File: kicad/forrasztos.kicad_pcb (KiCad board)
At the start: 2 copper layers, 90 parts, among them J1 24V+-, J2 Conn_01x04_Pin, J3 Conn_01x20_Pin, J4 Conn_01x06_Pin, J5 Conn_01x04_Pin, Q1 AOD409, Q2 MMST2222A, Q3 AOD409, Q4 MMST2222A, SW1 RotaryEncoder_Switch, SW2 SW_Push, SW3 SW_Push, U1 AP63205WU, U2 MCP6004, U3 AP63203WU, U4 24LC00, U5 STM32F103C8Tx, Y1 ATS080B

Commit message: redone pcb
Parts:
- removed the C13 at (153.3, 94.8)
- removed the C14 at (153.3, 90.2)
- removed the C15 at (145.3, 83.0)
- removed the C16 at (143.3, 87.0)
- removed the R6 at (162.6, 86.7)
- removed the R7 at (159.8, 86.8)
- added C13: 100n, Capacitor_SMD:C_0805_2012Metric_Pad1.18x1.45mm_HandSolder, F.Cu at (97.8, 86.4)
- added C13: 100n, Capacitor_SMD:C_0805_2012Metric_Pad1.18x1.45mm_HandSolder, F.Cu at (145.9, 90.6)
- added C14: 100n, Capacitor_SMD:C_0805_2012Metric_Pad1.18x1.45mm_HandSolder, F.Cu at (97.8, 89.4)
- added C14: 100n, Capacitor_SMD:C_0805_2012Metric_Pad1.18x1.45mm_HandSolder, F.Cu at (147.9, 80.4)
- added C15: 100n, Capacitor_SMD:C_0805_2012Metric_Pad1.18x1.45mm_HandSolder, F.Cu at (97.8, 92.4)
- added C15: 100n, Capacitor_SMD:C_0805_2012Metric_Pad1.18x1.45mm_HandSolder, F.Cu at (137.5, 77.1)
- added C16: 100n, Capacitor_SMD:C_0805_2012Metric_Pad1.18x1.45mm_HandSolder, F.Cu at (97.8, 95.4)
- added C16: 100n, Capacitor_SMD:C_0805_2012Metric_Pad1.18x1.45mm_HandSolder, F.Cu at (134.4, 79.4)
- added R42: 82k, Resistor_SMD:R_0805_2012Metric_Pad1.20x1.40mm_HandSolder, F.Cu at (156.3, 101.5)
- added R43: 33K, Resistor_SMD:R_0805_2012Metric_Pad1.20x1.40mm_HandSolder, F.Cu at (156.3, 104.5)
- added R44: 1.5K, Resistor_SMD:R_0805_2012Metric_Pad1.20x1.40mm_HandSolder, F.Cu at (147.9, 98.8)
- added R6: 4k7, Resistor_SMD:R_0805_2012Metric_Pad1.20x1.40mm_HandSolder, F.Cu at (155.3, 90.6)
- added R6: 4k7, Resistor_SMD:R_0805_2012Metric_Pad1.20x1.40mm_HandSolder, F.Cu at (102.6, 86.3)
- added R7: 4k7, Resistor_SMD:R_0805_2012Metric_Pad1.20x1.40mm_HandSolder, F.Cu at (102.6, 89.3)
- added R7: 4k7, Resistor_SMD:R_0805_2012Metric_Pad1.20x1.40mm_HandSolder, F.Cu at (153.2, 90.6)
- C11, C12, FB2, J1, R12, R17, R38, R41: moved to F.Cu
- J2, J5: footprint Connector_PinHeader_2.54mm:PinHeader_1x04_P2.54mm_Vertical -> Connector_PinHeader_2.54mm:PinHeader_2x04_P2.54mm_Vertical
- moved R2 169.4 mm to (176.3, 95.6), turned to 90 degrees
- moved J1 168.3 mm to (202.6, 81.5)
- moved R1 166.8 mm to (171.9, 95.6), turned to 90 degrees
- moved R3 166.2 mm to (174.2, 95.6), turned to 90 degrees
- moved C7 145.8 mm to (187.4, 70.1), turned to 90 degrees
- moved RV1 145.5 mm to (194.3, 72.4)
- moved C8 144.9 mm to (186.1, 74.0), turned to 90 degrees
- moved J5 143.9 mm to (173.5, 118.6), turned to -90 degrees
- moved C2 143.0 mm to (176.8, 74.0)
- moved C3 137.4 mm to (172.2, 73.8), turned to 90 degrees
- moved C4 133.9 mm to (169.6, 73.8), turned to 90 degrees
- moved C18 132.4 mm to (172.3, 86.6), turned to 180 degrees
- moved C1 129.5 mm to (160.5, 74.4), turned to 180 degrees
- moved C17 128.9 mm to (172.3, 84.3), turned to 180 degrees
- moved Q3 124.7 mm to (241.7, 71.7)
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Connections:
- REF** pad 1: (no net) -> Earth_Protective
- U5 pad 18: unconnected-(U5-PB0-Pad18) -> /LCD_CS1
- U5 pad 19: unconnected-(U5-PB1-Pad19) -> /LCD_CS2
- U5 pad 29: /LCD_CS1 -> /LCD_E
- U5 pad 30: /LCD_CS2 -> /LCD_RW
- U5 pad 31: /LCD_E -> /LCD_DI
- U5 pad 32: /LCD_RW -> /USB_DM
- U5 pad 33: /LCD_DI -> /USB_DP
- U5 pad 38: unconnected-(U5-PA15-Pad38) -> /USB_SNS
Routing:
- net GND: track 203.4 -> 388.4 mm, vias 9 -> 10
- net +5V: track 7.14 -> 117.2 mm, vias 0 -> 1
- net /ENC_B: track 0.00 -> 81.9 mm, vias 0 -> 2
- net /ENC_A: track 0.00 -> 81.2 mm, vias 0 -> 2
- net /ENC_SW: track 9.98 -> 87.7 mm, vias 0 -> 2
- net /LCD_VOUT: track 0.00 -> 69.8 mm, vias 0 -> 1
- net /CH2_AMP_N: track 59.6 -> 0.00 mm, vias 3 -> 0
- net /LCD_D2: track 5.43 -> 56.5 mm, vias 0 -> 1
- net /LCD_DI: track 0.00 -> 50.1 mm, vias 0 -> 1
- net /LCD_RST: track 6.50 -> 56.6 mm, vias 0 -> 1
- net /LCD_RW: track 0.00 -> 47.6 mm, vias 0 -> 1
- net /LCD_D3: track 4.60 -> 52.1 mm, vias 0 -> 1
- net /LCD_E: track 0.00 -> 46.7 mm, vias 0 -> 1
- net /LCD_V0: track 0.00 -> 45.7 mm, vias 0 -> 1
- net /LCD_D7: track 0.00 -> 42.0 mm, vias 0 -> 1
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
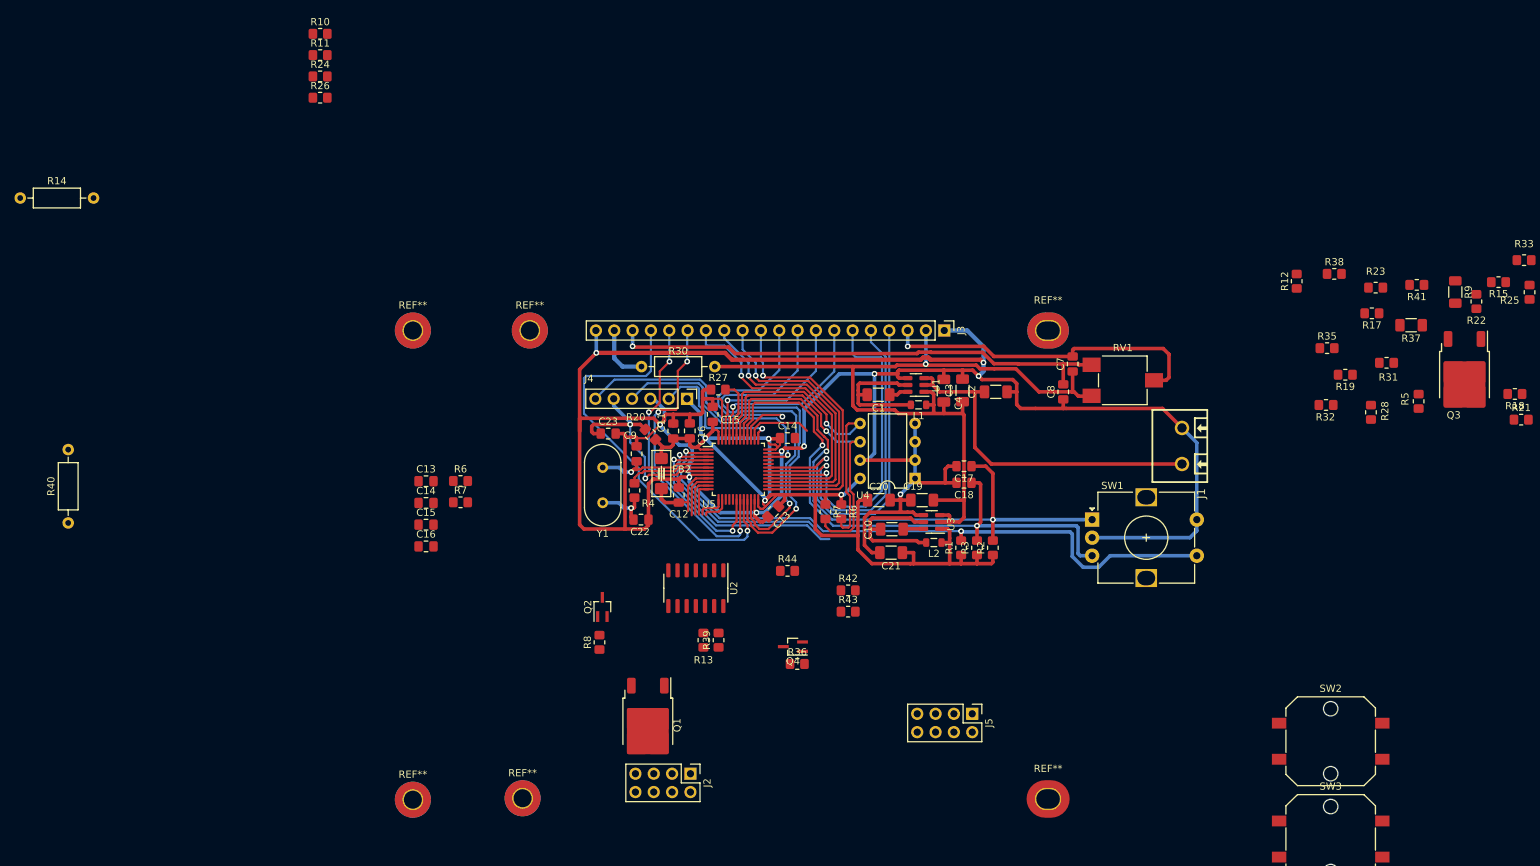
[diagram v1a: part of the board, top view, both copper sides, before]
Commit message: fixed footprints, power part done
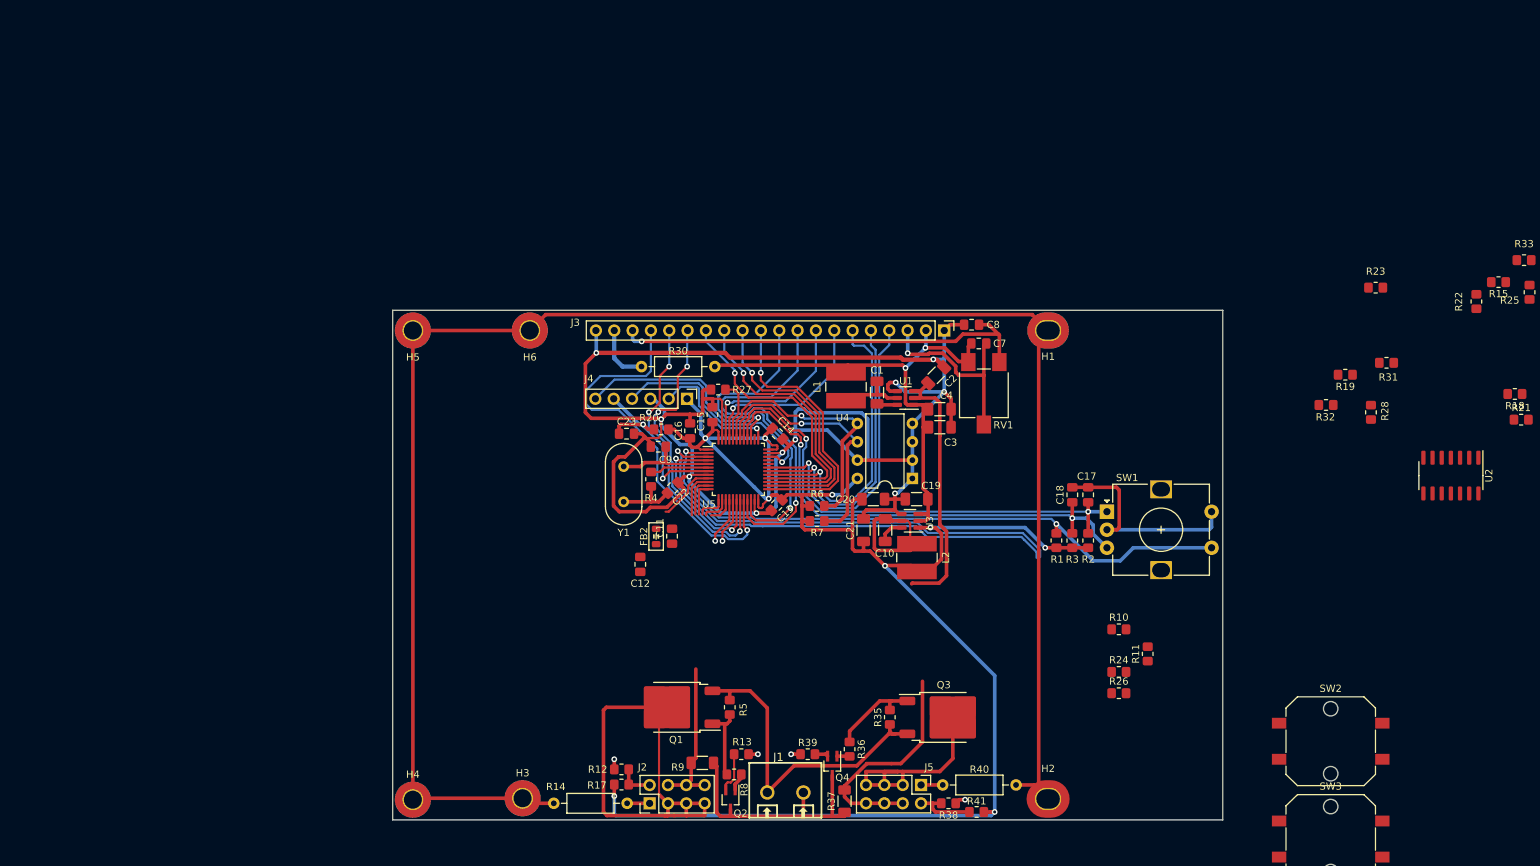
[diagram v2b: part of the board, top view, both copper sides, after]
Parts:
- removed the C13 at (145.9, 90.6)
- removed the C14 at (147.9, 80.4)
- removed the C15 at (137.5, 77.1)
- removed the C16 at (134.4, 79.4)
- removed R42: 82k, Resistor_SMD:R_0805_2012Metric_Pad1.20x1.40mm_HandSolder
- removed R43: 33K, Resistor_SMD:R_0805_2012Metric_Pad1.20x1.40mm_HandSolder
- removed R44: 1.5K, Resistor_SMD:R_0805_2012Metric_Pad1.20x1.40mm_HandSolder
- removed the R6 at (155.3, 90.6)
- removed the R7 at (153.2, 90.6)
- removed REF** (x4): MountingHole_2.5mm_Pad_TopBottom, MountingHole:MountingHole_2.5mm_Pad_TopBottom
- removed REF**: MountingHoleOval_3.27x2.7mm, forrasztos_library:MountingHoleOval_3.27x2.7mm
- removed REF**: MountingHoleOval_3.27x2.5mm, forrasztos_library:MountingHoleOval_3.27x2.5mm
- added H1: MountingHole_Pad, forrasztos_library:MountingHoleOval_3.27x2.5mm, F.Cu at (184.0, 65.5)
- added H2: MountingHole_Pad, forrasztos_library:MountingHoleOval_3.27x2.7mm, F.Cu at (184.0, 130.4)
- added H3: MountingHole_Pad, MountingHole:MountingHole_2.5mm_Pad_TopBottom, F.Cu at (111.2, 130.3)
- added H4: MountingHole_Pad, MountingHole:MountingHole_2.5mm_Pad_TopBottom, F.Cu at (96.0, 130.5)
- added H5: MountingHole_Pad, MountingHole:MountingHole_2.5mm_Pad_TopBottom, F.Cu at (96.0, 65.5)
- added H6: MountingHole_Pad, MountingHole:MountingHole_2.5mm_Pad_TopBottom, F.Cu at (112.2, 65.5)
- FB2: footprint PCM_Ferrite_SMD_Handsoldering_AKL:Ferrite_1806_4516Metric_Pad1.57x1.80mm_BigPads -> PCM_Ferrite_SMD_Handsoldering_AKL:Ferrite_0805_2012Metric
- J2, J5: value Conn_01x04_Pin -> Conn_02x04_Pin
- L1, L2: footprint Inductor_SMD:L_0805_2012Metric -> Inductor_SMD:L_TracoPower_TCK-047_5.2x5.8mm
- Q1, Q3: footprint Library:TO-252-2-custom -> forrasztos_library:TO-252-2-custom
- moved R11 141.5 mm to (197.8, 110.3), turned to 90 degrees
- moved R10 138.0 mm to (193.8, 106.9)
- moved R24 138.0 mm to (193.8, 112.8)
- moved R26 138.0 mm to (193.8, 115.8)
- moved R40 136.2 mm to (179.6, 128.5), turned to 180 degrees
- moved R9 123.0 mm to (136.1, 125.4), turned to 180 degrees
- moved R17 122.8 mm to (124.9, 128.4)
- moved R12 115.4 mm to (124.9, 126.3), turned to 0 degrees
- moved R14 111.8 mm to (115.5, 131.0)
- moved U2 105.8 mm to (239.8, 85.6)
- moved R5 104.4 mm to (139.9, 117.7), turned to -90 degrees
- moved R37 102.5 mm to (155.8, 130.7), turned to 90 degrees
- moved R41 95.1 mm to (174.1, 132.2), turned to 0 degrees
- moved R38 90.8 mm to (170.2, 131.0), turned to 180 degrees
- moved Q3 86.3 mm to (169.5, 119.1), turned to 0 degrees
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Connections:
- J2 pad 1: /CH1_AMP_P -> Net-(J2-Pin_3)
- J2 pad 3: Net-(J2-Pin_3) -> /CH1_AMP_P
- J2 pad 4: Net-(J2-Pin_4) -> /CH1_AMP_N
- J2 pad 5: (no net) -> /CH1_AMP_P
- J2 pad 6: (no net) -> /CH1_AMP_N
- J2 pad 7: (no net) -> /CH1_AMP_P
- J2 pad 8: (no net) -> /CH1_AMP_N
- J5 pad 1: /CH2_AMP_P -> Net-(J5-Pin_3)
- J5 pad 2: /CH2_AMP_N -> Net-(J5-Pin_4)
- J5 pad 3: Net-(J5-Pin_3) -> /CH2_AMP_P
- J5 pad 4: Net-(J5-Pin_4) -> /CH2_AMP_N
- J5 pad 5: (no net) -> /CH2_AMP_P
- J5 pad 6: (no net) -> /CH2_AMP_N
- J5 pad 7: (no net) -> /CH2_AMP_P
- J5 pad 8: (no net) -> /CH2_AMP_N
- U5 pad 32: /USB_DM -> unconnected-(U5-PA11-Pad32)
- U5 pad 33: /USB_DP -> unconnected-(U5-PA12-Pad33)
- U5 pad 38: /USB_SNS -> unconnected-(U5-PA15-Pad38)
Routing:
- net Earth_Protective: track 0.00 -> 245.9 mm
- net +3.3V: track 137.7 -> 239.4 mm, vias 4 -> 9
- net /CH1_AMP_P: track 0.00 -> 62.1 mm
- net GND: track 388.4 -> 341.7 mm
- net +5V: track 117.2 -> 72.1 mm, vias 1 -> 2
- net +24V: track 48.2 -> 83.2 mm
- net /BTN_1: track 31.8 -> 64.0 mm
- net /CH2_AMP_N: track 0.00 -> 31.7 mm
- net /CH2_AMP_P: track 0.00 -> 31.0 mm
- net /BTN_2: track 32.8 -> 63.0 mm
- net /CH1_AMP_N: track 0.00 -> 21.7 mm
- net /LCD_V0: track 45.7 -> 26.9 mm
- net /ENC_B: track 81.9 -> 69.0 mm
- net Net-(Q3-G): track 0.00 -> 12.5 mm
- net Net-(Q1-G): track 0.00 -> 10.6 mm
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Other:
- board outline added: 115 x 70.6 mm

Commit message: finished work on pcb
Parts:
- SW2, SW3: footprint Button_Switch_SMD:SW_Push_1P1T_NO_CK_PTS125Sx43PSMTR -> Button_Switch_THT:SW_PUSH-12mm
- moved R16 157.3 mm to (104.3, 103.3), turned to 90 degrees
- moved R25 155.7 mm to (100.8, 102.1), turned to 180 degrees
- moved R34 153.9 mm to (105.7, 106.2), turned to 180 degrees
- moved R15 149.7 mm to (99.7, 88.5)
- moved R29 149.4 mm to (107.6, 104.2)
- moved R33 148.8 mm to (108.5, 102.1)
- moved R22 148.8 mm to (100.8, 104.1), turned to 0 degrees
- moved R21 140.6 mm to (110.3, 97.8), turned to 90 degrees
- moved R18 140.1 mm to (109.5, 90.6), turned to 0 degrees
- moved U2 135.7 mm to (104.6, 97.3)
- moved R31 132.1 mm to (100.7, 92.5), turned to 180 degrees
- moved R28 129.7 mm to (99.7, 90.5), turned to 180 degrees
- moved R19 128.9 mm to (101.0, 106.1)
- moved R23 125.3 mm to (108.5, 92.6), turned to 0 degrees
- moved R32 125.3 mm to (99.0, 97.0), turned to -90 degrees
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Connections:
- J2 pad 1: Net-(J2-Pin_3) -> /CH1_AMP_P
- J2 pad 2: Net-(J2-Pin_4) -> /CH1_AMP_N
- J2 pad 3: /CH1_AMP_P -> Net-(J2-Pin_3)
- J2 pad 4: /CH1_AMP_N -> Net-(J2-Pin_4)
- J5 pad 1: Net-(J5-Pin_3) -> /CH2_AMP_P
- J5 pad 2: Net-(J5-Pin_4) -> /CH2_AMP_N
- J5 pad 3: /CH2_AMP_P -> Net-(J5-Pin_3)
- J5 pad 4: /CH2_AMP_N -> Net-(J5-Pin_4)
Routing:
- net GND: track 341.7 -> 754.3 mm, vias 10 -> 14
- net Earth_Protective: track 245.9 -> 613.2 mm
- net +3.3V: track 239.4 -> 428.1 mm, vias 9 -> 11
- net /CH2_AMP_P: track 31.0 -> 103.2 mm, vias 0 -> 53
- net /CH2_AMP_N: track 31.7 -> 98.4 mm, vias 0 -> 2
- net /CH2_TILT: track 7.98 -> 73.1 mm
- net /CH1_AMP_N: track 21.7 -> 82.7 mm, vias 0 -> 2
- net /CH1_TILT: track 8.27 -> 68.7 mm
- net /CH1_CURRENT: track 4.06 -> 60.8 mm, vias 0 -> 2
- net +5V: track 72.1 -> 117.9 mm, vias 2 -> 1
- net /CH2_THERMO: track 4.03 -> 49.5 mm, vias 0 -> 2
- net /CH1_THERMO: track 5.20 -> 48.9 mm
- net /CH2_HEATER: track 7.24 -> 48.9 mm, vias 1 -> 2
- net +3.3VA: track 8.47 -> 46.1 mm, vias 0 -> 2
- net /CH2_CURRENT: track 3.79 -> 40.0 mm, vias 0 -> 2
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- added copper zone on F.Cu, net +24V
- added copper zone on B.Cu, net +3.3V
- added copper zone on F.Cu, net +3.3V
- added copper zone on F.Cu, net +5V
- added copper zone on B.Cu, net /CH1_AMP_P
- added copper zone on F.Cu, net /CH1_AMP_P
- added copper zone on B.Cu, net /CH2_AMP_P
- added copper zone on F.Cu, net /CH2_AMP_P
- added copper zone on B.Cu, net Earth_Protective
- added copper zone on B.Cu, net GND
- added copper zone on F.Cu, net GND

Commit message: revA prototype
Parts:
- added NT1: NetTie_2, NetTie:NetTie-2_SMD_Pad0.5mm, B.Cu at (147.8, 128.9)
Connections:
- H1 pad 1: Earth_Protective -> GND
- H2 pad 1: Earth_Protective -> GND
- H3 pad 1: Earth_Protective -> GND
- H4 pad 1: Earth_Protective -> GND
- H5 pad 1: Earth_Protective -> GND
- H6 pad 1: Earth_Protective -> GND
- Q2 pad 3: GND -> GNDPWR
- Q4 pad 3: GND -> GNDPWR
- R14 pad 1: Earth_Protective -> GND
- R37 pad 1: GND -> GNDPWR
- R40 pad 1: Earth_Protective -> GND
- R9 pad 1: GND -> GNDPWR
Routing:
- net Earth_Protective: track 613.2 -> 0.00 mm
- net GND: track 754.3 -> 1286.5 mm, vias 14 -> 79
- net GNDPWR: track 0.00 -> 40.6 mm, vias 0 -> 1
- net /BTN_2: track 95.9 -> 88.9 mm
- net /BTN_1: track 75.4 -> 69.5 mm
- net Net-(Q4-C): track 3.16 -> 1.76 mm
- net Net-(Q4-B): track 3.26 -> 1.86 mm
- removed copper zone on B.Cu, net Earth_Protective
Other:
- board text added: "Elkövető: Jakab Ádám"
- board text added: "SEM forrasztoállomás Rev.A"

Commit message: start port of PTDreamer repo
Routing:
- added copper zone on F.Cu, net GNDPWR
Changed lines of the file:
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@@
   (segment (start 140.5 121.7) (end 141.5 120.7) (width 0.5) (layer "B.Cu") (net 54))
   (segment (start 138.2 130.3) (end 139.7 131.8) (width 1) (layer "F.Cu") (net 55))
-  (segment (start 155.35 131.8) (end 155.8 132.25) (width 1) (layer "F.Cu") (net 55))
   (segment (start 139.7 131.8) (end 140 131.8) (width 1) (layer "F.Cu") (net 55))
   (segment (start 138.2 127.45) (end 138.2 130.3) (width 1) (layer "F.Cu") (net 55))
   (segment (start 154.1 128.481496) (end 154.1 127.13) (width 1) (layer "F.Cu") (net 55))
+  (segment (start 153.65 131.8) (end 154.1 132.25) (width 1) (layer "F.Cu") (net 55))
   (segment (start 137.7 126.95) (end 138.2 127.45) (width 1) (layer "F.Cu") (net 55))
   (segment (start 137.7 126.95) (end 137.7 125.45) (width 1) (layer "F.Cu") (net 55))
+  (segment (start 154.1 132.25) (end 155.8 132.25) (width 1) (layer "F.Cu") (net 55))
   (segment (start 137.7 125.45) (end 137.65 125.4) (width 1) (layer "F.Cu") (net 55))
   (segment (start 139.7 131.8) (end 150.781496 131.8) (width 1) (layer "F.Cu") (net 55))
-  (segment (start 150.781496 131.8) (end 155.35 131.8) (width 1) (layer "F.Cu") (net 55))
+  (segment (start 150.781496 131.8) (end 153.65 131.8) (width 1) (layer "F.Cu") (net 55))
   (segment (start 150.781496 131.8) (end 154.1 128.481496) (width 1) (layer "F.Cu") (net 55))
   (via (at 137.7 126.95) (size 0.8) (drill 0.4) (layers "F.Cu" "B.Cu") (net 55))
@@
     )
   )
-  (zone (net 11) (net_name "+3.3V") (layer "F.Cu") (hatch full 0.5)
+  (zone (net 11) (net_name "+3.3V") (layer "F.Cu") (hatch edge 0.5)
     (priority 2)
     (connect_pads (clearance 0.5))
@@
     )
   )
-  (zone (net 11) (net_name "+3.3V") (layer "F.Cu") (hatch full 0.5)
+  (zone (net 11) (net_name "+3.3V") (layer "F.Cu") (hatch edge 0.5)
     (priority 2)
     (connect_pads yes (clearance 0.5))
@@
     )
   )
-  (zone (net 4) (net_name "GND") (layer "F.Cu") (hatch full 0.5)
-    (priority 20)
-    (connect_pads (clearance 0.5))
-    (min_thickness 0.25) (filled_areas_thickness no)
-    (fill yes (thermal_gap 0.5) (thermal_bridge_width 0.5))
-    (polygon
-      (pts
-        (xy 164.2 77)
-        (xy 166.4 77)
-        (xy 166.4 71.5)
-        (xy 164.2 69.3)
-      )
-    )
-  )
   (zone (net 0) (net_name "") (layer "F.Cu") (name "enc_keepout") (hatch full 0.5)
     (connect_pads (clearance 0))
@@
     )
   )
-  (zone (net 4) (net_name "GND") (layer "F.Cu") (hatch full 0.5)
+  (zone (net 4) (net_name "GND") (layer "F.Cu") (hatch edge 0.5)
     (priority 12)
     (connect_pads (clearance 0.5))
@@
     )
   )
-  (zone (net 3) (net_name "+24V") (layer "F.Cu") (hatch full 0.5)
+  (zone (net 3) (net_name "+24V") (layer "F.Cu") (hatch edge 0.5)
     (connect_pads yes (clearance 0.5))
     (min_thickness 0.25) (filled_areas_thickness no)
@@
     )
   )
-  (zone (net 17) (net_name "/CH1_AMP_P") (layer "F.Cu") (hatch full 0.5)
+  (zone (net 17) (net_name "/CH1_AMP_P") (layer "F.Cu") (hatch edge 0.5)
     (priority 33)
     (connect_pads yes (clearance 0.5))
@@
     )
   )
-  (zone (net 11) (net_name "+3.3V") (layer "F.Cu") (hatch full 0.5)
+  (zone (net 11) (net_name "+3.3V") (layer "F.Cu") (hatch edge 0.5)
     (priority 2)
     (connect_pads yes (clearance 0.5))
@@
     )
   )
-  (zone (net 4) (net_name "GND") (layer "F.Cu") (hatch full 0.5)
+  (zone (net 55) (net_name "GNDPWR") (layer "F.Cu") (hatch full 0.5)
     (priority 10)
-    (connect_pads (clearance 0.5))
-    (min_thickness 0.25) (filled_areas_thickness no)
-    (fill yes (thermal_gap 0.5) (thermal_bridge_width 0.5))
-    (polygon
-      (pts
-        (xy 152.8 126.3)
-        (xy 154.3 126.3)
-        (xy 154.3 133)
-        (xy 152.8 133)
-      )
-    )
-  )
-  (zone (net 3) (net_name "+24V") (layer "F.Cu") (hatch full 0.5)
+    (connect_pads yes (clearance 0.5))
+    (min_thickness 0.25) (filled_areas_thickness no)
+    (fill yes (thermal_gap 0.5) (thermal_bridge_width 0.5))
+    (polygon
+      (pts
+        (xy 151.95 126.05)
+        (xy 156.95 126.05)
+        (xy 156.95 133.3)
+        (xy 151.95 133.3)
+      )
+    )
+  )
+  (zone (net 3) (net_name "+24V") (layer "F.Cu") (hatch edge 0.5)
     (priority 1)
     (connect_pads yes (clearance 0.5))
@@
     )
   )
-  (zone (net 39) (net_name "/CH2_AMP_P") (layer "F.Cu") (hatch full 0.5)
+  (zone (net 39) (net_name "/CH2_AMP_P") (layer "F.Cu") (hatch edge 0.5)
     (priority 32)
     (connect_pads yes (clearance 0.5))
@@
     )
   )
-  (zone (net 39) (net_name "/CH2_AMP_P") (layer "B.Cu") (hatch full 0.5)
+  (zone (net 39) (net_name "/CH2_AMP_P") (layer "B.Cu") (hatch edge 0.5)
     (priority 32)
     (connect_pads yes (clearance 0.5))
@@
     )
   )
-  (zone (net 4) (net_name "GND") (layer "B.Cu") (hatch full 0.5)
+  (zone (net 4) (net_name "GND") (layer "B.Cu") (hatch edge 0.5)
     (priority 4)
     (connect_pads yes (clearance 0.5))
@@
     )
   )
-  (zone (net 17) (net_name "/CH1_AMP_P") (layer "B.Cu") (hatch full 0.5)
+  (zone (net 17) (net_name "/CH1_AMP_P") (layer "B.Cu") (hatch edge 0.5)
     (priority 33)
     (connect_pads yes (clearance 0.5))
